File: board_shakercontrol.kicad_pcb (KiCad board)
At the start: 2 copper layers, 104.6 x 66.5 mm, 21 parts, among them J1 Power, J2 Power, J3 control / 5V, J4 Shaker, Q1 IRF640NS, U1 L7805, U2 LTV-817

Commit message: Minor changes
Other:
- board text added: "+"
- board text added: "-"
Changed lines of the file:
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@@
     (property "Sheetname" "")
     (attr through_hole)
-    (fp_text reference "D1" (at 7.7 3.3) (layer "F.SilkS")
+    (fp_text reference "D1" (at 18.064 -2.698) (layer "F.SilkS")
       (effects (font (size 1 1) (thickness 0.15)))
     )
@@
     (fp_line (start -0.562893 0) (end -1.27 0.5) (layer "F.Fab") (width 0.1))
     (fp_line (start 6.35 -2.92) (end -1.27 -2.92) (layer "F.Fab") (width 0.1))
-    (pad "1" thru_hole roundrect (at 0 0 180) (size 1.74 2.19) (drill 1.19) (layers *.Cu *.Mask) (roundrect_rratio 0.143678)
+    (pad "1" thru_hole roundrect (at 0 0 180) (size 1.74 2.19) (drill 1.19) (layers *.Cu *.Mask) (roundrect_rratio 0.1436781609)
       (net 1 "GND") (pinfunction "Pin_1") (pintype "passive"))
     (pad "2" thru_hole oval (at 2.54 0 180) (size 1.74 2.19) (drill 1.19) (layers *.Cu *.Mask)
@@
     (fp_line (start 15.845 3.895) (end 15.845 4.9) (layer "F.Fab") (width 0.1))
     (fp_line (start -0.005 3.895) (end -1.91 3.895) (layer "F.Fab") (width 0.1))
-    (pad "1" thru_hole roundrect (at 0 0 180) (size 3.16 4.1) (drill 1.7) (layers *.Cu *.Mask) (roundrect_rratio 0.079114)
+    (pad "1" thru_hole roundrect (at 0 0 180) (size 3.16 4.1) (drill 1.7) (layers *.Cu *.Mask) (roundrect_rratio 0.07911392405)
       (net 2 "Net-(J1-Pad1)") (pinfunction "Pin_1") (pintype "passive"))
     (pad "2" thru_hole oval (at 3.96 0 180) (size 3.16 4.1) (drill 1.7) (layers *.Cu *.Mask)
@@
     (fp_line (start -1.91 3.895) (end -1.91 -5.11) (layer "F.Fab") (width 0.1))
     (fp_line (start -1.91 -5.11) (end 17.75 -5.11) (layer "F.Fab") (width 0.1))
-    (pad "1" thru_hole roundrect (at 0 0 180) (size 3.16 4.1) (drill 1.7) (layers *.Cu *.Mask) (roundrect_rratio 0.079114)
+    (pad "1" thru_hole roundrect (at 0 0 180) (size 3.16 4.1) (drill 1.7) (layers *.Cu *.Mask) (roundrect_rratio 0.07911392405)
       (net 2 "Net-(J1-Pad1)") (pinfunction "Pin_1") (pintype "passive"))
     (pad "2" thru_hole oval (at 3.96 0 180) (size 3.16 4.1) (drill 1.7) (layers *.Cu *.Mask)
@@
     (fp_line (start -1.202893 0) (end -1.91 0.5) (layer "F.Fab") (width 0.1))
     (fp_line (start 5.87 3.895) (end 3.965 3.895) (layer "F.Fab") (width 0.1))
-    (pad "1" thru_hole roundrect (at 0 0 180) (size 3.16 4.1) (drill 1.7) (layers *.Cu *.Mask) (roundrect_rratio 0.079114)
+    (pad "1" thru_hole roundrect (at 0 0 180) (size 3.16 4.1) (drill 1.7) (layers *.Cu *.Mask) (roundrect_rratio 0.07911392405)
       (net 13 "Net-(J4-Pad1)") (pinfunction "Pin_1") (pintype "passive"))
     (pad "2" thru_hole oval (at 3.96 0 180) (size 3.16 4.1) (drill 1.7) (layers *.Cu *.Mask)
@@
     (effects (font (size 1 1) (thickness 0.15)))
   )
+  (gr_text "-" (at 68.834 85.344) (layer "F.SilkS")
+    (effects (font (size 1.5 1.5) (thickness 0.3)))
+  )
   (gr_text "5V CTL GND" (at 135.382 101.346) (layer "F.SilkS")
     (effects (font (size 1 1) (thickness 0.15)))
   )
+  (gr_text "+" (at 94.488 85.344) (layer "F.SilkS")
+    (effects (font (size 1.5 1.5) (thickness 0.3)))
+  )
   (segment (start 109.68622 59.69) (end 100.03422 69.342) (width 1.016) (layer "F.Cu") (net 1))

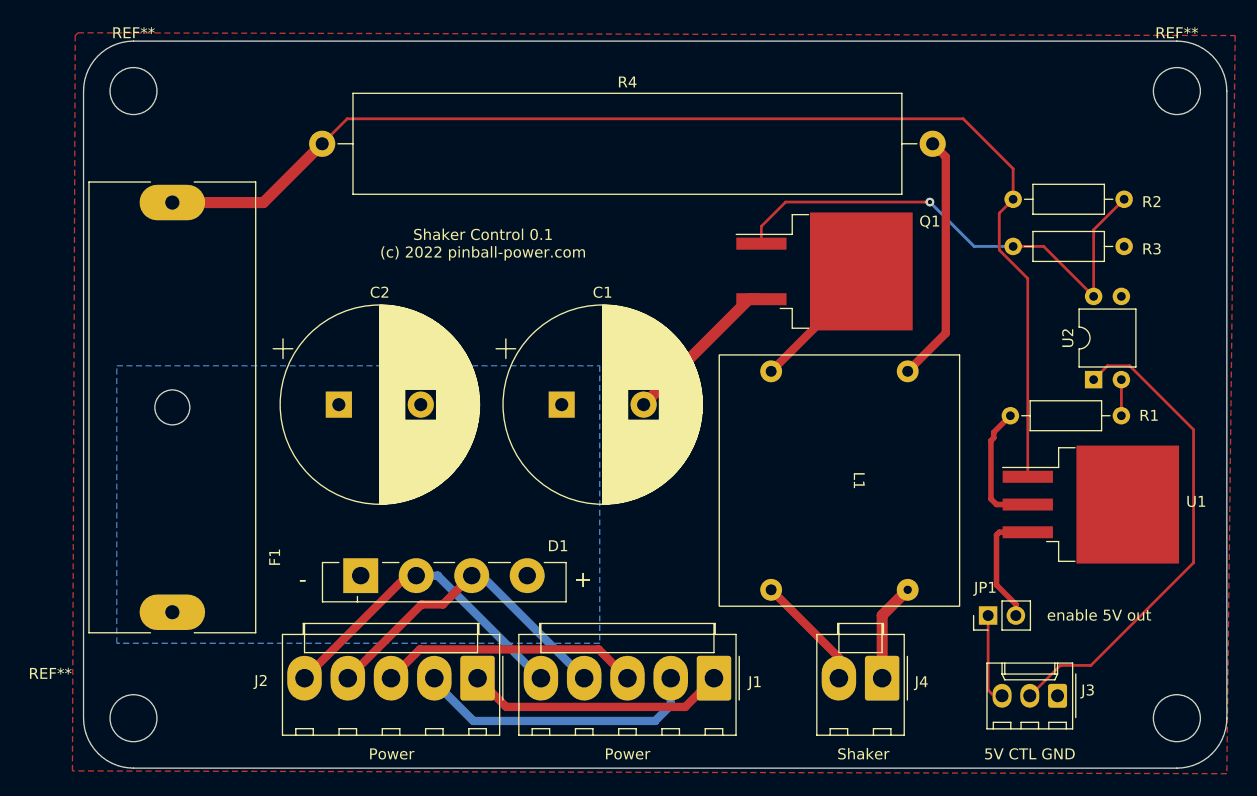
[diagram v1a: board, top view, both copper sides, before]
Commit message: Slightly reduced board size
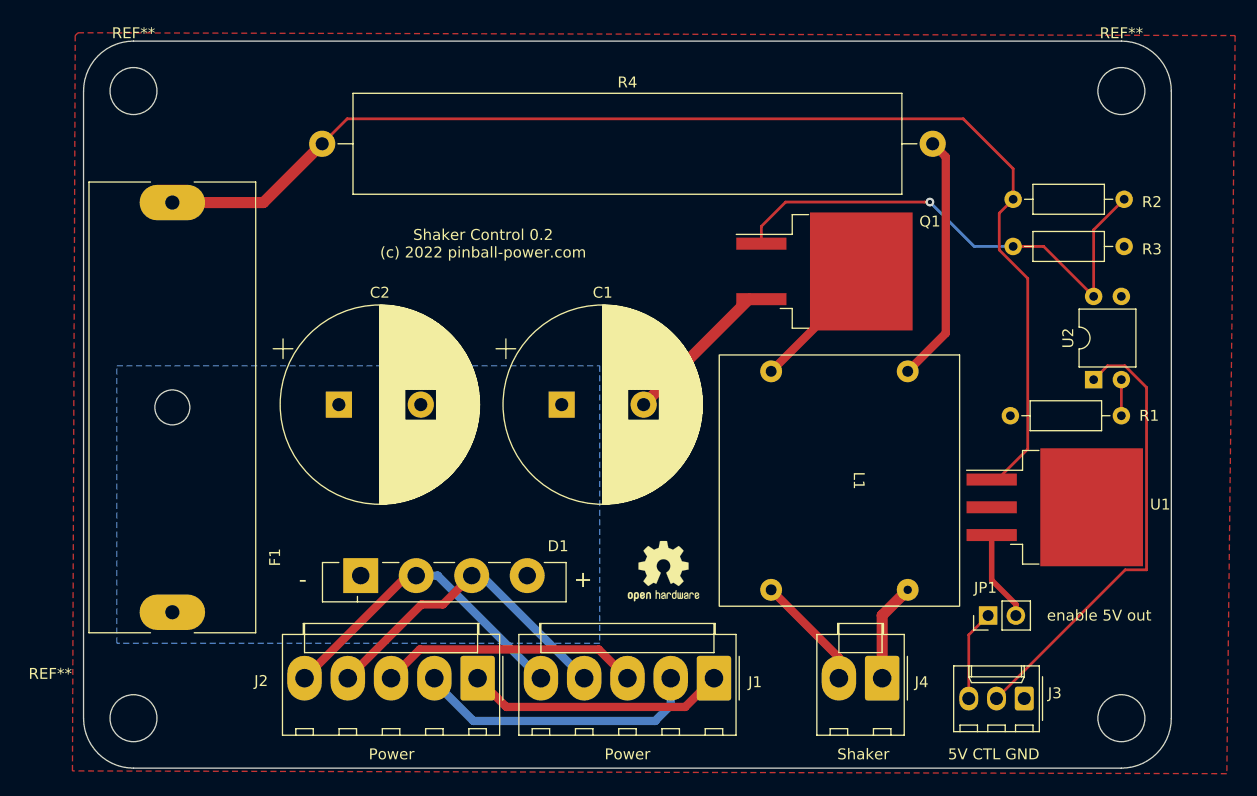
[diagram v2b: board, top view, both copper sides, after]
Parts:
- added REF**: OSHW-Logo2_7.3x6mm_SilkScreen, Symbol:OSHW-Logo2_7.3x6mm_SilkScreen, F.Cu at (101.9, 84.6)
- R1: value 330R -> 100R
- moved REF** 5.08 mm to (143.8, 40.6)
- moved REF** 5.08 mm to (143.8, 98.0)
- moved U1 3.31 mm to (137.7, 78.7)
- moved J3 3.06 mm to (134.9, 96.2)
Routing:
- net GND: track 26.7 -> 14.8 mm
- net Net-(J3-Pad2): track 45.1 -> 41.5 mm
- net +5V: track 11.1 -> 8.29 mm
- net VCC: track 111.8 -> 113.2 mm
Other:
- board size 104.6 x 66.5 mm -> 99.6 x 66.5 mm
- board text added: "Shaker Control 0.2 (c) 2022 pinball-power.com"
- board text removed: "Shaker Control 0.1 (c) 2022 pinball-power.com"
